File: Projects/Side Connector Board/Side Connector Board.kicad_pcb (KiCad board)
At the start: 2 copper layers, 156.5 x 22.6 mm, 18 parts, among them J1 Conn_02x09_Odd_Even, J2 Conn_02x09_Odd_Even, J3 Conn_02x09_Odd_Even, J4 Conn_02x09_Odd_Even, P1 CONN_02X04, P10 CONN_02X04, P2 CONN_02X04, P3 CONN_02X04, P4 CONN_02X04, P5 CONN_02X04, P6 CONN_02X04, P7 CONN_02X04, P8 CONN_02X04, P9 CONN_02X04

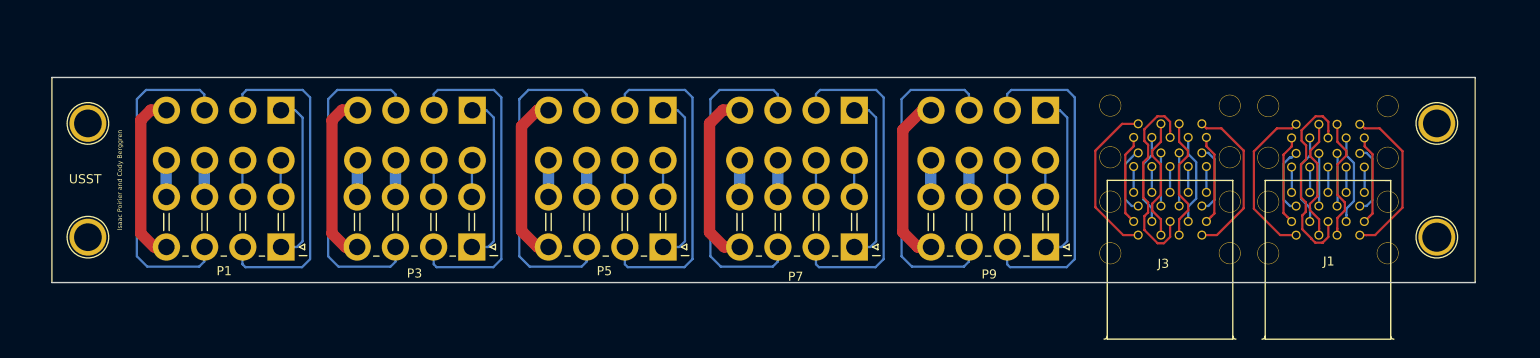
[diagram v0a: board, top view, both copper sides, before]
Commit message: Slight changes to PCB panel
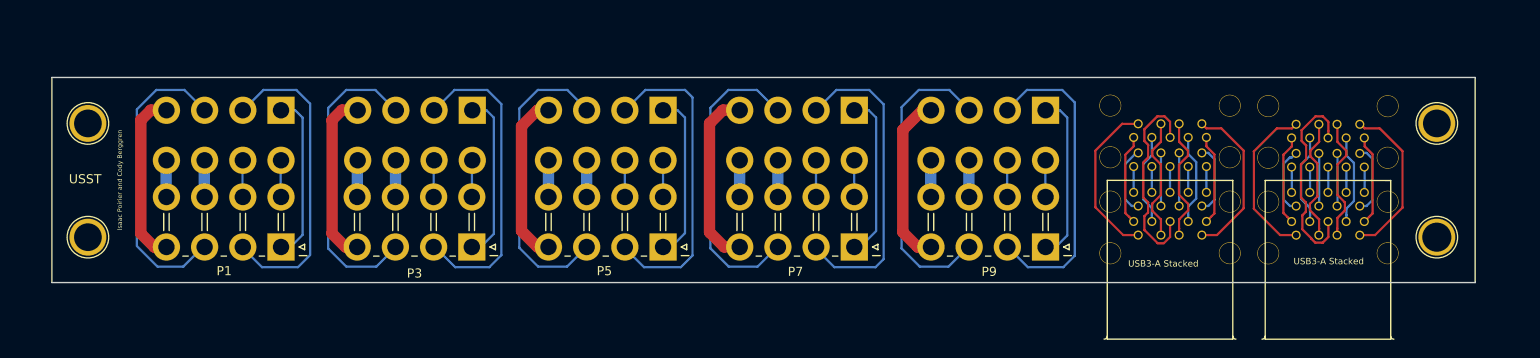
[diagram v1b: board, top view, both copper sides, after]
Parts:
- USB3-A Stacked: renamed from J1
- USB3-A Stacked: renamed from J2
- USB3-A Stacked: renamed from J3
- USB3-A Stacked: renamed from J4
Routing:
- net Net-(P1-Pad3): track 36.8 -> 33.5 mm
- net Net-(P5-Pad3): track 36.8 -> 33.7 mm
- net Net-(P7-Pad3): track 36.8 -> 33.7 mm
- net Net-(P3-Pad3): track 36.8 -> 33.8 mm
- net Net-(P10-Pad3): track 36.8 -> 33.8 mm
- net Net-(P3-Pad2): track 37.4 -> 34.5 mm
- net Net-(P1-Pad2): track 37.4 -> 34.6 mm
- net Net-(P10-Pad2): track 37.4 -> 34.7 mm
- net Net-(P7-Pad2): track 37.4 -> 34.9 mm
- net Net-(P5-Pad2): track 37.4 -> 35.0 mm
- net Net-(P7-Pad1): track 19.0 -> 18.4 mm
- net Net-(P5-Pad1): track 19.0 -> 18.5 mm

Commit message: Added form factor for drill holes & useful silkscreens to PCB panels
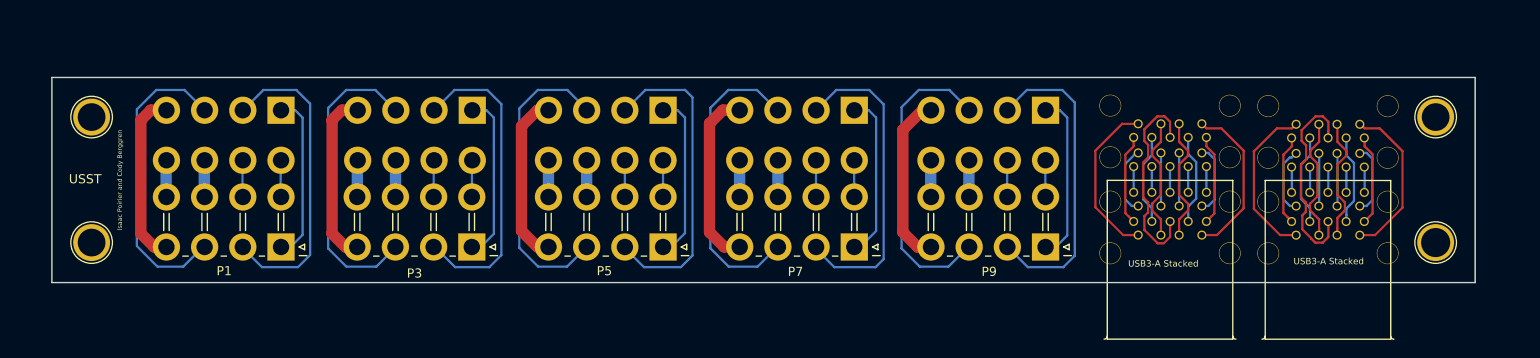
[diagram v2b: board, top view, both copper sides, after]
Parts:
- moved REF** 0.81 mm to (73.0, 96.0)
- moved REF** 0.72 mm to (73.0, 109.8)
- moved REF** 0.71 mm to (220.8, 96.0)
- moved REF** 0.61 mm to (220.8, 109.8)
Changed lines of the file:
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@@
   )
   (module Connect:1pin (layer F.Cu)
-    (at 72.5932 96.6978)
+    (at 73 96)
     (descr "module 1 pin (ou trou mecanique de percage)")
     (tags DEV)
@@
   )
   (module Connect:1pin (layer F.Cu)
-    (at 72.5932 109.2073)
+    (at 73 109.8)
     (descr "module 1 pin (ou trou mecanique de percage)")
     (tags DEV)
@@
   )
   (module Connect:1pin (layer F.Cu)
-    (at 220.9292 109.2073)
+    (at 220.8 109.8)
     (descr "module 1 pin (ou trou mecanique de percage)")
     (tags DEV)
@@
   )
   (module Connect:1pin (layer F.Cu)
-    (at 220.9292 96.6978)
+    (at 220.8 96)
     (descr "module 1 pin (ou trou mecanique de percage)")
     (tags DEV)

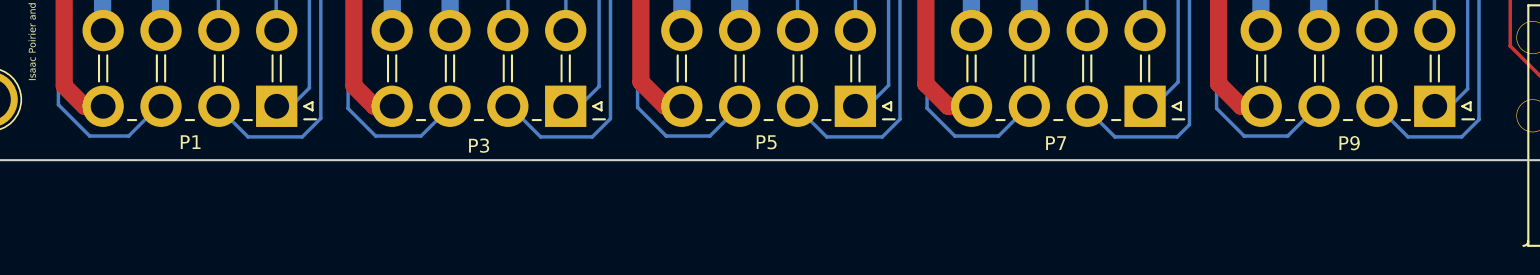
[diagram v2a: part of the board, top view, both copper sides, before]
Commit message: Added silkscreen for 2x4 molex connectors
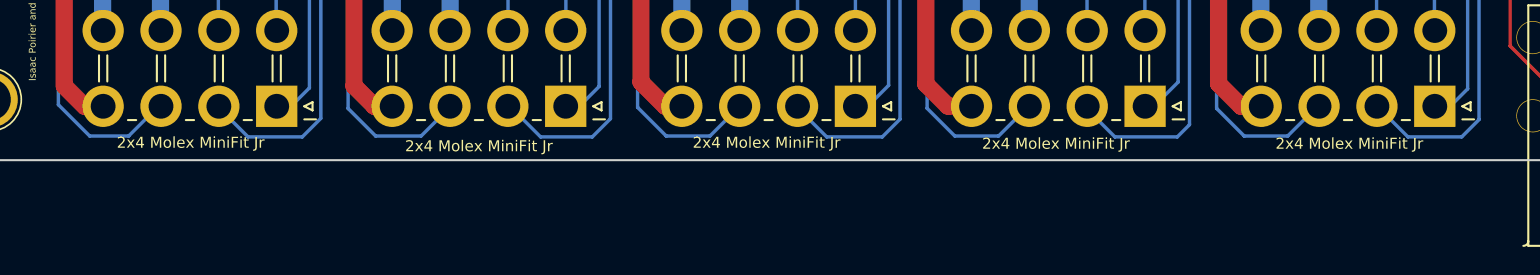
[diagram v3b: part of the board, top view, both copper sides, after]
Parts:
- 2x4 Molex MiniFit Jr: renamed from P1
- 2x4 Molex MiniFit Jr: renamed from P3
- 2x4 Molex MiniFit Jr: renamed from P5
- 2x4 Molex MiniFit Jr: renamed from P7
- 2x4 Molex MiniFit Jr: renamed from P9
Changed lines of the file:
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@@
     (descr "Molex Mini-Fit JR, PN:5569-08A2, dual row, side entry type, through hole, with plastic peg mount")
     (tags "connector molex mini-fit 5569")
-    (fp_text reference P1 (at 6.2484 -2.6416 180) (layer F.SilkS)
-      (effects (font (size 1 1) (thickness 0.15)))
+    (fp_text reference "2x4 Molex MiniFit Jr" (at 6.2484 -2.6416 180) (layer F.SilkS)
+      (effects (font (size 0.8 0.8) (thickness 0.15)))
     )
     (fp_text value CONN_02X04 (at 6.7056 -7.9248 180) (layer F.Fab)
@@
     (descr "Molex Mini-Fit JR, PN:5569-08A2, dual row, side entry type, through hole, with plastic peg mount")
     (tags "connector molex mini-fit 5569")
-    (fp_text reference P3 (at 6.2992 -2.8956 180) (layer F.SilkS)
-      (effects (font (size 1 1) (thickness 0.15)))
+    (fp_text reference "2x4 Molex MiniFit Jr" (at 6.2992 -2.8956 180) (layer F.SilkS)
+      (effects (font (size 0.8 0.8) (thickness 0.15)))
     )
     (fp_text value CONN_02X04 (at 6.1976 -7.9756 180) (layer F.Fab)
@@
     (descr "Molex Mini-Fit JR, PN:5569-08A2, dual row, side entry type, through hole, with plastic peg mount")
     (tags "connector molex mini-fit 5569")
-    (fp_text reference P5 (at 6.4516 -2.6416 180) (layer F.SilkS)
-      (effects (font (size 1 1) (thickness 0.15)))
+    (fp_text reference "2x4 Molex MiniFit Jr" (at 6.4516 -2.6416 180) (layer F.SilkS)
+      (effects (font (size 0.8 0.8) (thickness 0.15)))
     )
     (fp_text value CONN_02X04 (at 6.096 -7.7724 180) (layer F.Fab)
@@
     (descr "Molex Mini-Fit JR, PN:5569-08A2, dual row, side entry type, through hole, with plastic peg mount")
     (tags "connector molex mini-fit 5569")
-    (fp_text reference P7 (at 6.4704 -2.7132 180) (layer F.SilkS)
-      (effects (font (size 1 1) (thickness 0.15)))
+    (fp_text reference "2x4 Molex MiniFit Jr" (at 6.4704 -2.7132 180) (layer F.SilkS)
+      (effects (font (size 0.8 0.8) (thickness 0.15)))
     )
     (fp_text value CONN_02X04 (at 5.9436 -7.8232 180) (layer F.Fab)
@@
     (descr "Molex Mini-Fit JR, PN:5569-08A2, dual row, side entry type, through hole, with plastic peg mount")
     (tags "connector molex mini-fit 5569")
-    (fp_text reference P9 (at 6.2016 -2.7132 180) (layer F.SilkS)
-      (effects (font (size 1 1) (thickness 0.15)))
+    (fp_text reference "2x4 Molex MiniFit Jr" (at 6.2016 -2.7132 180) (layer F.SilkS)
+      (effects (font (size 0.8 0.8) (thickness 0.15)))
     )
     (fp_text value CONN_02X04 (at 6.2484 -7.5692 180) (layer F.Fab)

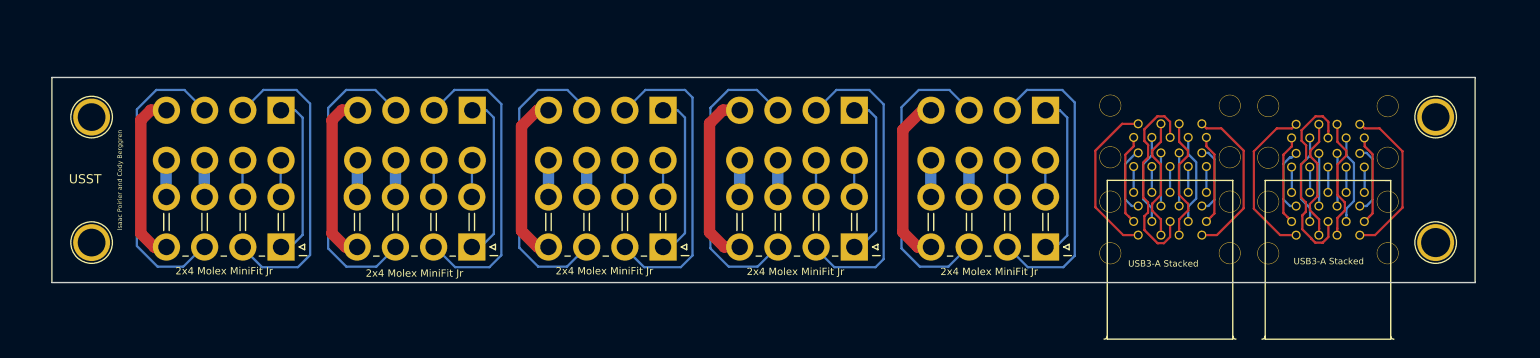
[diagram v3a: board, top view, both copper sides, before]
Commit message: Slight refactor of Side connector board(mounting holes, overall size)
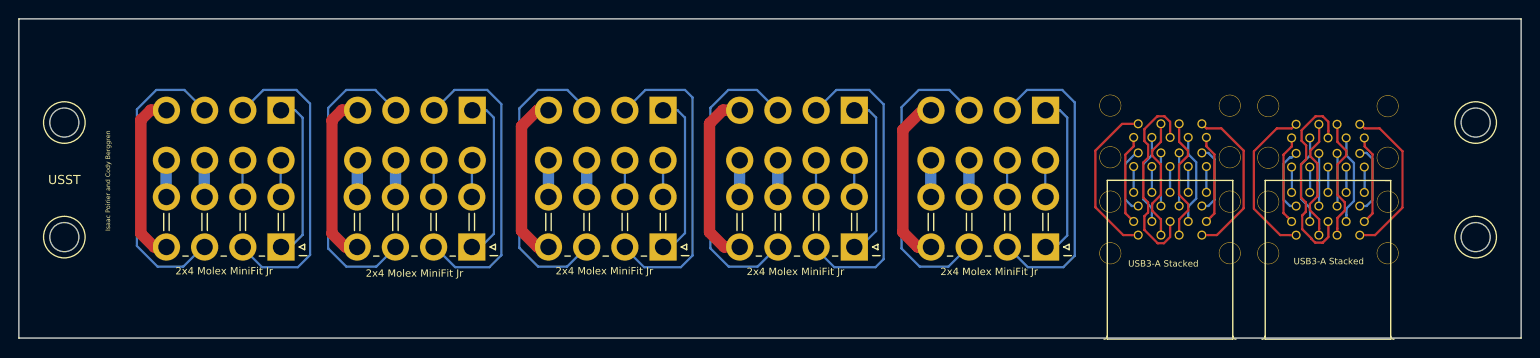
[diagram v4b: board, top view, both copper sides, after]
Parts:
- moved REF** 4.44 mm to (225.2, 96.6)
- moved REF** 4.44 mm to (225.2, 109.2)
- moved REF** 3.06 mm to (70.0, 96.6)
- moved REF** 3.06 mm to (70.0, 109.2)
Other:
- board size 156.5 x 22.6 mm -> 165.2 x 35.1 mm
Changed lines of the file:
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@@
     (links 76)
     (no_connects 0)
-    (area 68.555799 91.568199 225.220601 114.273401)
+    (area 64.924999 91.524999 230.275001 114.275001)
     (thickness 1.6)
     (drawings 6)
@@
     (mod_text_size 1 1)
     (mod_text_width 0.15)
-    (pad_size 4.064 4.064)
-    (pad_drill 3.048)
+    (pad_size 3.2 3.2)
+    (pad_drill 3.2)
     (pad_to_mask_clearance 0.2)
     (aux_axis_origin 0 0)
@@
   )
   (module Connect:1pin (layer F.Cu)
-    (at 73 96)
+    (at 225.2 96.6)
     (descr "module 1 pin (ou trou mecanique de percage)")
     (tags DEV)
@@
       (effects (font (size 1 1) (thickness 0.15)))
     )
-    (fp_text value 1pin (at 0 3) (layer F.Fab)
+    (fp_text value 1pin (at 0 3) (layer F.Fab) hide
       (effects (font (size 1 1) (thickness 0.15)))
     )
@@
     (fp_circle (center 0 0) (end 2.6 0) (layer F.CrtYd) (width 0.05))
     (fp_circle (center 0 0) (end 0 -2.286) (layer F.SilkS) (width 0.12))
-    (pad "" np_thru_hole circle (at 0 0) (size 4.064 4.064) (drill 3.048) (layers *.Cu *.Mask))
+    (pad "" np_thru_hole circle (at 0 0) (size 3.2 3.2) (drill 3.2) (layers *.Cu *.Mask))
   )
   (module Connect:1pin (layer F.Cu)
-    (at 73 109.8)
+    (at 70 96.6)
     (descr "module 1 pin (ou trou mecanique de percage)")
     (tags DEV)
@@
     (fp_circle (center 0 0) (end 2.6 0) (layer F.CrtYd) (width 0.05))
     (fp_circle (center 0 0) (end 0 -2.286) (layer F.SilkS) (width 0.12))
-    (pad "" np_thru_hole circle (at 0 0) (size 4.064 4.064) (drill 3.048) (layers *.Cu *.Mask))
+    (pad "" np_thru_hole circle (at 0 0) (size 3.2 3.2) (drill 3.2) (layers *.Cu *.Mask))
   )
   (module Connect:1pin (layer F.Cu)
-    (at 220.8 109.8)
+    (at 70 109.2)
     (descr "module 1 pin (ou trou mecanique de percage)")
     (tags DEV)
@@
     (fp_circle (center 0 0) (end 2.6 0) (layer F.CrtYd) (width 0.05))
     (fp_circle (center 0 0) (end 0 -2.286) (layer F.SilkS) (width 0.12))
-    (pad "" np_thru_hole circle (at 0 0) (size 4.064 4.064) (drill 3.2) (layers *.Cu *.Mask))
+    (pad "" np_thru_hole circle (at 0 0) (size 3.2 3.2) (drill 3.2) (layers *.Cu *.Mask))
   )
   (module Connect:1pin (layer F.Cu)
-    (at 220.8 96)
+    (at 225.2 109.2)
     (descr "module 1 pin (ou trou mecanique de percage)")
     (tags DEV)
@@
     (fp_circle (center 0 0) (end 2.6 0) (layer F.CrtYd) (width 0.05))
     (fp_circle (center 0 0) (end 0 -2.286) (layer F.SilkS) (width 0.12))
-    (pad "" np_thru_hole circle (at 0 0) (size 4.064 4.064) (drill 3.048) (layers *.Cu *.Mask))
+    (pad "" np_thru_hole circle (at 0 0) (size 3.2 3.2) (drill 3.2) (layers *.Cu *.Mask))
   )
   (module USST-footprints:USB-A_3.0_Stacked_WM10420-ND (layer F.Cu)
@@
     )
   )
-  (gr_text USST (at 72.2884 102.8192) (layer F.SilkS)
+  (gr_text USST (at 70 102.9) (layer F.SilkS)
     (effects (font (size 1 1) (thickness 0.25)))
   )
-  (gr_line (start 225.1456 91.6432) (end 68.6308 91.6432) (angle 90) (layer Edge.Cuts) (width 0.15))
-  (gr_line (start 225.1456 114.1984) (end 225.1456 91.6432) (angle 90) (layer Edge.Cuts) (width 0.15))
-  (gr_line (start 68.6308 114.1984) (end 225.1456 114.1984) (angle 90) (layer Edge.Cuts) (width 0.15))
-  (gr_line (start 68.6308 91.6432) (end 68.6308 114.1984) (angle 90) (layer Edge.Cuts) (width 0.15))
-  (gr_text "Isaac Poirier and Cody Berggren" (at 76.0984 102.9208 90) (layer F.SilkS)
+  (gr_line (start 230.2 85.2) (end 65 85.2) (angle 90) (layer Edge.Cuts) (width 0.15))
+  (gr_line (start 230.2 120.3) (end 230.2 85.2) (angle 90) (layer Edge.Cuts) (width 0.15))
+  (gr_line (start 65 120.3) (end 230.2 120.3) (angle 90) (layer Edge.Cuts) (width 0.15))
+  (gr_line (start 65 85.2) (end 65 120.3) (angle 90) (layer Edge.Cuts) (width 0.15))
+  (gr_text "Isaac Poirier and Cody Berggren" (at 74.8 103 90) (layer F.SilkS)
     (effects (font (size 0.5 0.5) (thickness 0.125)))
   )
